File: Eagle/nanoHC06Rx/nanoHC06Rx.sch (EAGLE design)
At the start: 45 parts, among them J10 Relay, J14 Relay, J17 Relay, J2 Relay, J20 Pixel, J22 IR Rx, J33 Relay, Q1 2N5088, Q2 2N5088, X1 53047-11

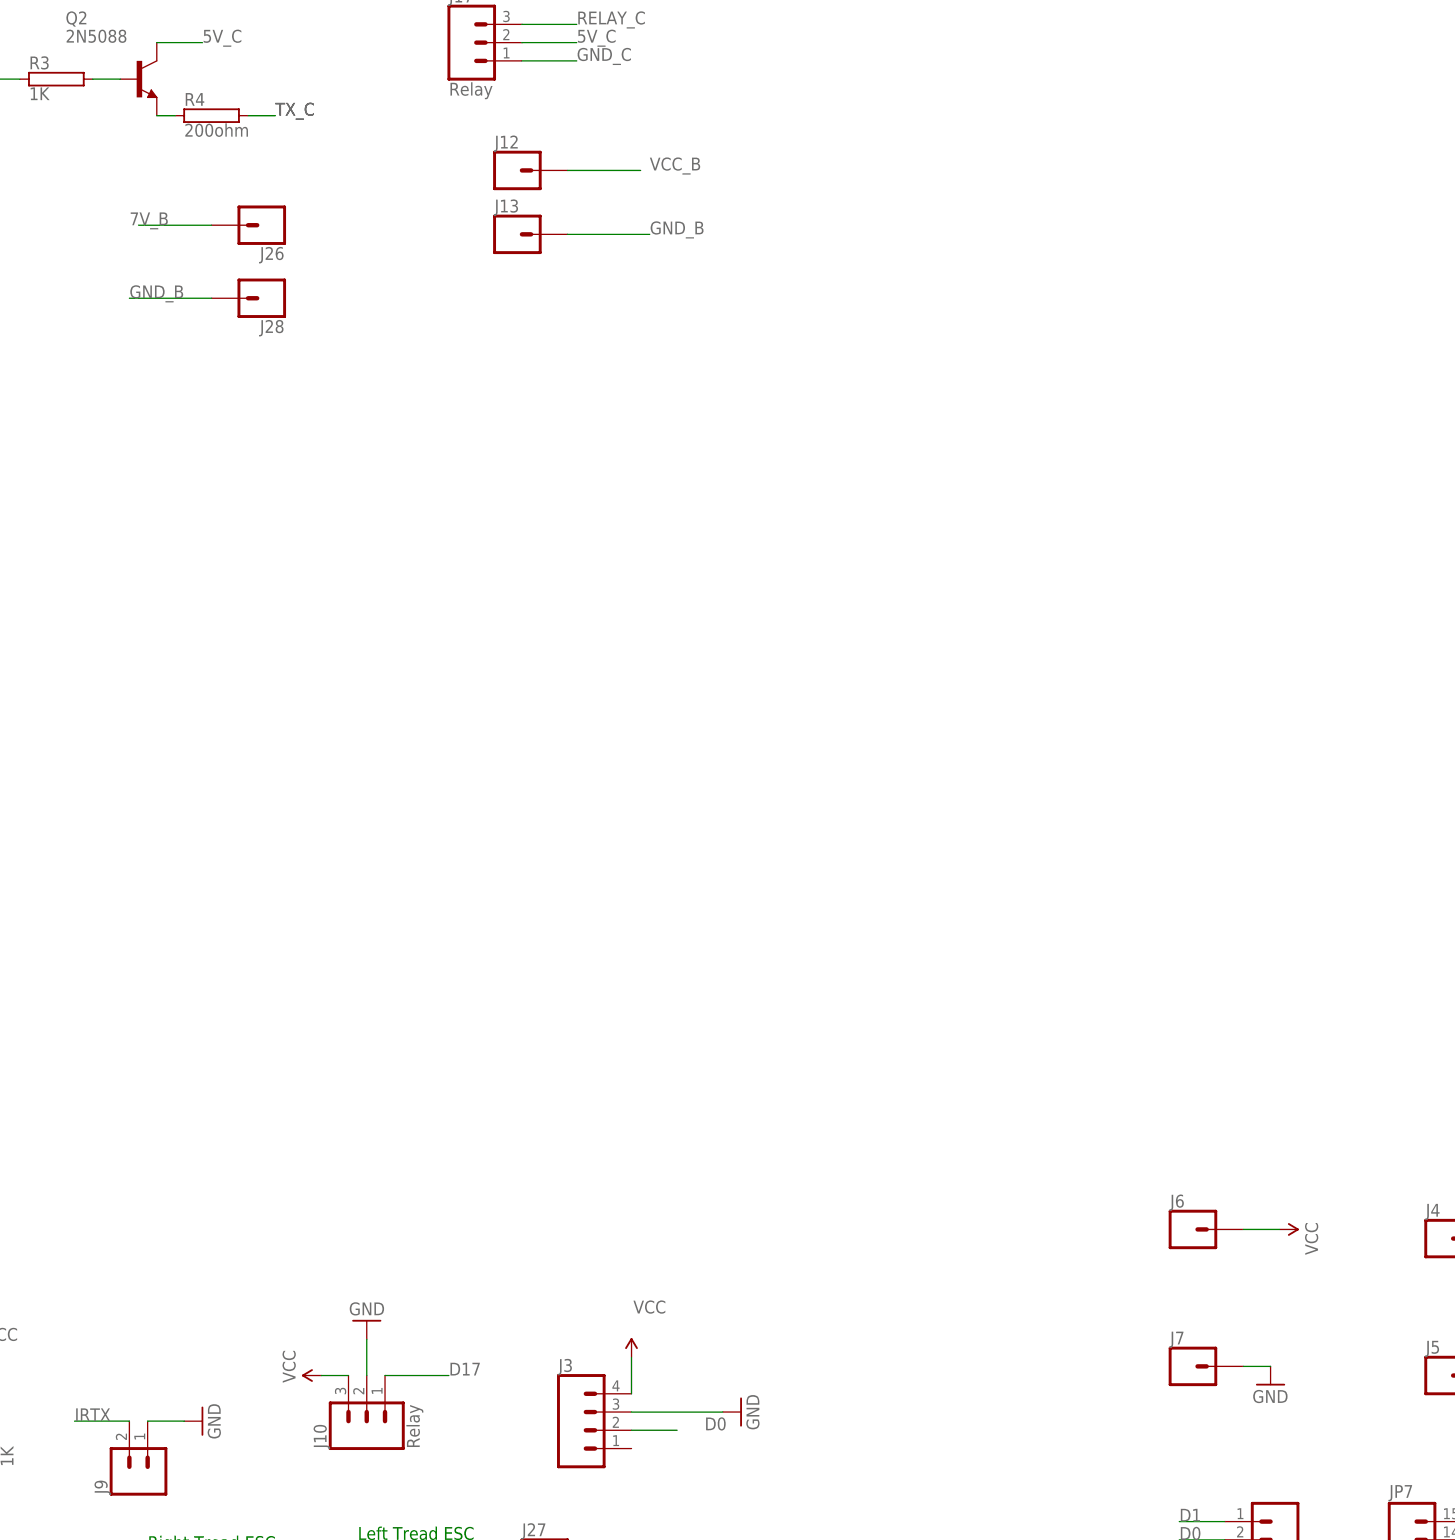
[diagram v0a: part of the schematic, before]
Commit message: Bind HC05 and HC06
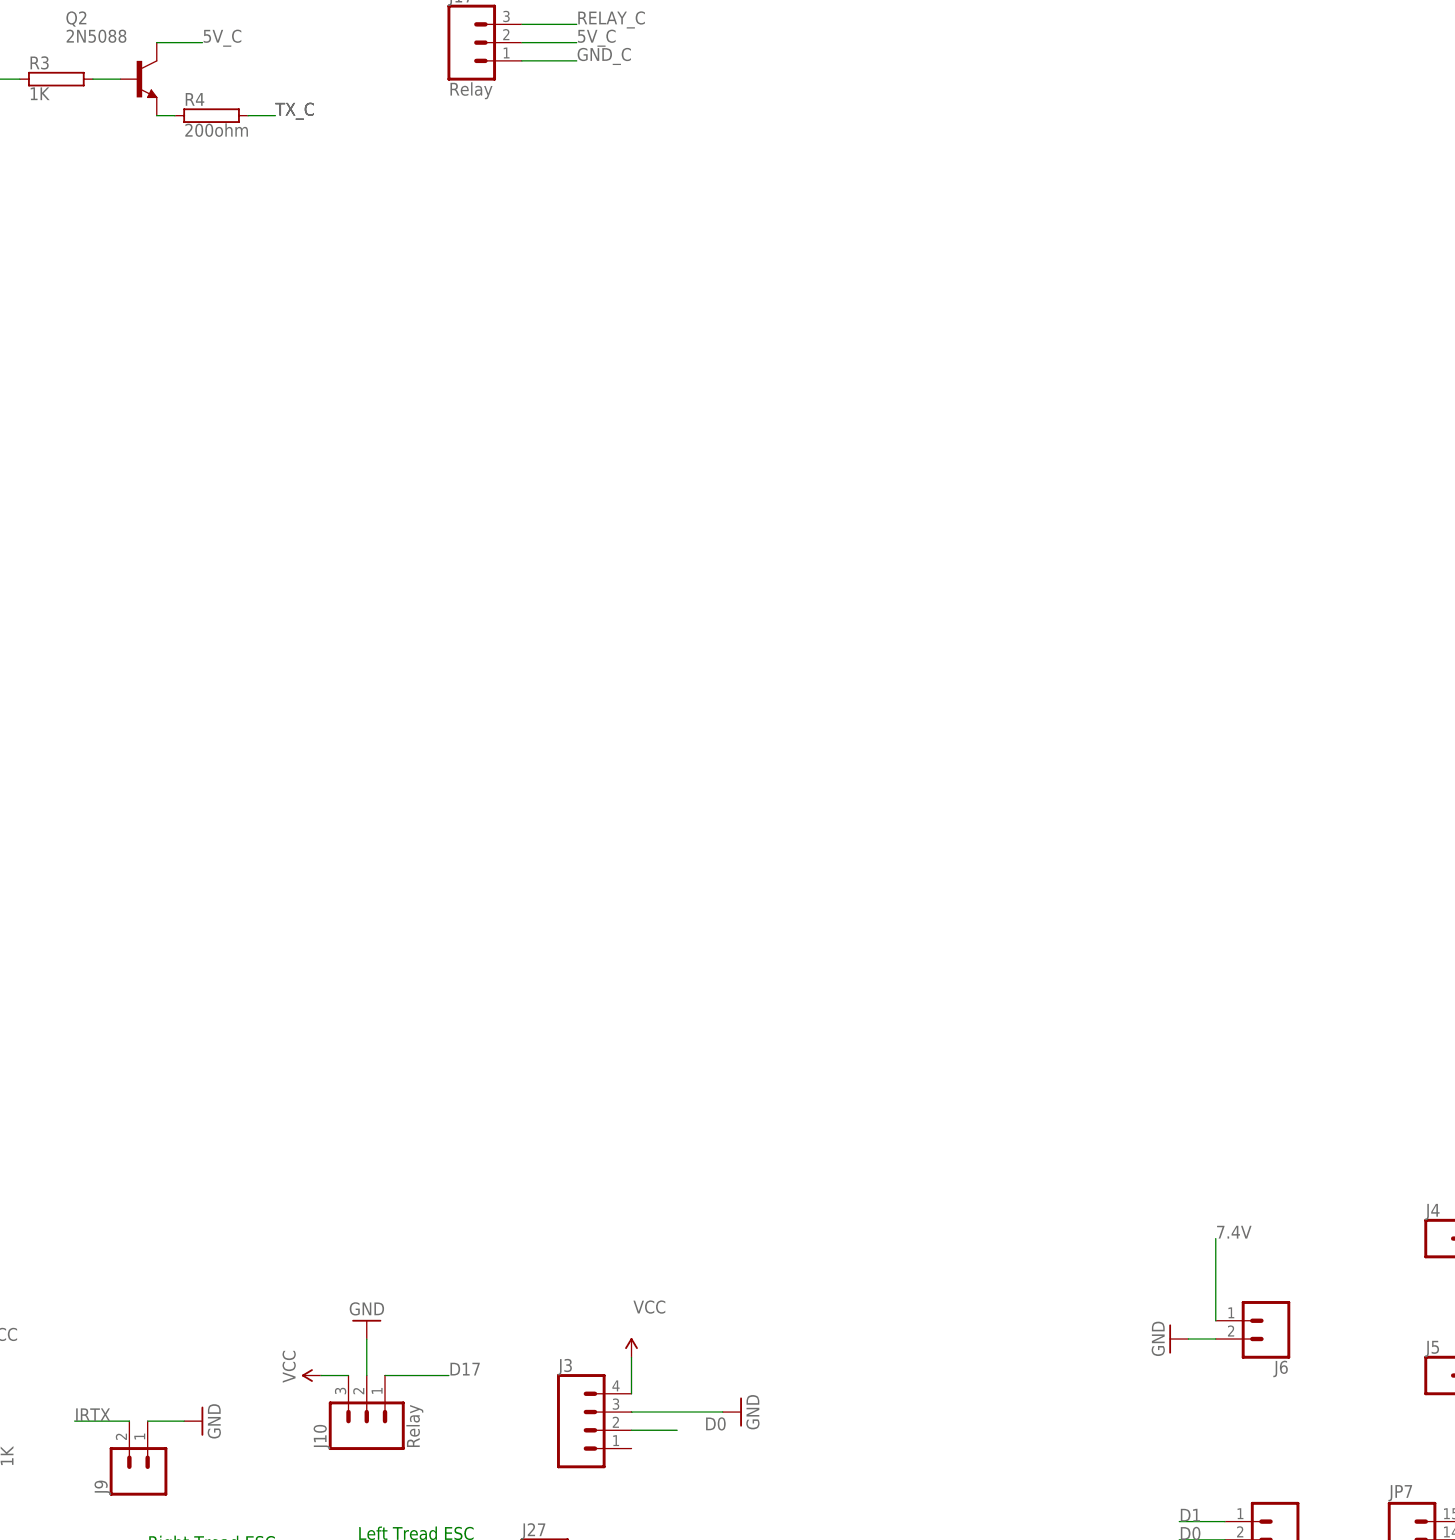
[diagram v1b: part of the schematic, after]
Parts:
- removed J12, J13, J26, J28, J7: (no value), SparkFun-Connectors:CONN_01
- J6: device SparkFun-Connectors:CONN_01 -> SparkFun-Connectors:CONN_02
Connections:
- removed net 7V_B: J26.1
- removed net GND_B: J13.1, J28.1
- removed net VCC_B: J12.1
- net 7.4V: now also J6.1
- net GND: now also J6.2; no longer J7.1
- net VCC: no longer J6.1
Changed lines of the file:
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@@
 <part name="J4" library="SparkFun-Connectors" library_urn="urn:adsk.eagle:library:513" deviceset="CONN_01" device="" package3d_urn="urn:adsk.eagle:package:38028/1"/>
 <part name="J5" library="SparkFun-Connectors" library_urn="urn:adsk.eagle:library:513" deviceset="CONN_01" device="" package3d_urn="urn:adsk.eagle:package:38028/1"/>
-<part name="J6" library="SparkFun-Connectors" library_urn="urn:adsk.eagle:library:513" deviceset="CONN_01" device="" package3d_urn="urn:adsk.eagle:package:38028/1"/>
-<part name="J7" library="SparkFun-Connectors" library_urn="urn:adsk.eagle:library:513" deviceset="CONN_01" device="" package3d_urn="urn:adsk.eagle:package:38028/1"/>
 <part name="GND6" library="SparkFun" deviceset="GND" device=""/>
-<part name="P+4" library="SparkFun" deviceset="VCC" device=""/>
-<part name="GND7" library="SparkFun" deviceset="GND" device=""/>
 <part name="JP3" library="SparkFun-Connectors" deviceset="M15" device=""/>
 <part name="JP4" library="SparkFun-Connectors" deviceset="M15" device=""/>
@@
 <part name="J32" library="SparkFun-Connectors" library_urn="urn:adsk.eagle:library:513" deviceset="CONN_10" device="&quot;" package3d_urn="urn:adsk.eagle:package:38157/1"/>
 <part name="J1" library="SparkFun-Connectors" library_urn="urn:adsk.eagle:library:513" deviceset="CONN_04" device="" package3d_urn="urn:adsk.eagle:package:38085/1"/>
-<part name="J12" library="SparkFun-Connectors" deviceset="CONN_01" device=""/>
-<part name="J13" library="SparkFun-Connectors" deviceset="CONN_01" device=""/>
 <part name="X1" library="con-molex" library_urn="urn:adsk.eagle:library:165" deviceset="53?-11" device="047" package3d_urn="urn:adsk.eagle:package:8078520/1"/>
 <part name="J16" library="SparkFun-Connectors" deviceset="CONN_06" device="NO_SILK_FEMALE_PTH"/>
@@
 <part name="J23" library="SparkFun-Connectors" library_urn="urn:adsk.eagle:library:513" deviceset="CONN_10" device="&quot;" package3d_urn="urn:adsk.eagle:package:38157/1"/>
 <part name="J24" library="SparkFun-Connectors" deviceset="CONN_08" device="&quot;"/>
-<part name="J26" library="SparkFun-Connectors" deviceset="CONN_01" device=""/>
-<part name="J28" library="SparkFun-Connectors" deviceset="CONN_01" device=""/>
 <part name="J29" library="SparkFun-Connectors" deviceset="CONN_06" device="NO_SILK_FEMALE_PTH"/>
 <part name="Q1" library="transistor-npn" library_urn="urn:adsk.eagle:library:398" deviceset="2N5088" device="" package3d_urn="urn:adsk.eagle:package:28523/2"/>
@@
 <part name="J14" library="SparkFun-Connectors" deviceset="CONN_03" device="" value="Relay"/>
 <part name="GND13" library="SparkFun" deviceset="GND" device=""/>
+<part name="J6" library="SparkFun-Connectors" deviceset="CONN_02" device=""/>
+<part name="GND7" library="SparkFun" deviceset="GND" device=""/>
 </parts>
 <sheets>
@@
 <attribute name="NAME" x="193.04" y="194.818" size="1.778" layer="95" font="vector"/>
 </instance>
-<instance part="J6" gate="G$1" x="160.02" y="212.09" smashed="yes">
-<attribute name="VALUE" x="157.48" y="207.264" size="1.778" layer="96" font="vector"/>
-<attribute name="NAME" x="157.48" y="215.138" size="1.778" layer="95" font="vector"/>
-</instance>
-<instance part="J7" gate="G$1" x="160.02" y="193.04" smashed="yes">
-<attribute name="VALUE" x="157.48" y="188.214" size="1.778" layer="96" font="vector"/>
-<attribute name="NAME" x="157.48" y="196.088" size="1.778" layer="95" font="vector"/>
-</instance>
 <instance part="GND6" gate="1" x="210.82" y="191.77" smashed="yes" rot="R90">
 <attribute name="VALUE" x="213.36" y="189.23" size="1.778" layer="96" rot="R90"/>
-</instance>
-<instance part="P+4" gate="1" x="172.72" y="212.09" smashed="yes" rot="R270">
-<attribute name="VALUE" x="176.276" y="213.106" size="1.778" layer="96" rot="R270"/>
-</instance>
-<instance part="GND7" gate="1" x="171.45" y="190.5" smashed="yes">
-<attribute name="VALUE" x="168.91" y="187.96" size="1.778" layer="96"/>
 </instance>
 <instance part="JP3" gate="G$1" x="261.62" y="353.06" smashed="yes" rot="R270">
@@
 <attribute name="NAME" x="249.682" y="401.32" size="1.778" layer="95" font="vector" rot="R90"/>
 </instance>
-<instance part="J12" gate="G$1" x="66.04" y="359.41" smashed="yes">
-<attribute name="VALUE" x="63.5" y="354.584" size="1.778" layer="96" font="vector"/>
-<attribute name="NAME" x="63.5" y="362.458" size="1.778" layer="95" font="vector"/>
-</instance>
-<instance part="J13" gate="G$1" x="66.04" y="350.52" smashed="yes">
-<attribute name="VALUE" x="63.5" y="345.694" size="1.778" layer="96" font="vector"/>
-<attribute name="NAME" x="63.5" y="353.568" size="1.778" layer="95" font="vector"/>
-</instance>
 <instance part="X1" gate="-1" x="38.1" y="410.21" smashed="yes">
 <attribute name="NAME" x="40.64" y="409.448" size="1.524" layer="95"/>
@@
 <attribute name="NAME" x="316.23" y="237.998" size="1.778" layer="95" font="vector"/>
 </instance>
-<instance part="J26" gate="G$1" x="31.75" y="351.79" smashed="yes" rot="R180">
-<attribute name="VALUE" x="34.29" y="356.616" size="1.778" layer="96" font="vector" rot="R180"/>
-<attribute name="NAME" x="34.29" y="348.742" size="1.778" layer="95" font="vector" rot="R180"/>
-</instance>
-<instance part="J28" gate="G$1" x="31.75" y="341.63" smashed="yes" rot="R180">
-<attribute name="VALUE" x="34.29" y="346.456" size="1.778" layer="96" font="vector" rot="R180"/>
-<attribute name="NAME" x="34.29" y="338.582" size="1.778" layer="95" font="vector" rot="R180"/>
-</instance>
 <instance part="J29" gate="G$1" x="43.18" y="137.16" smashed="yes" rot="R270">
 <attribute name="VALUE" x="33.274" y="142.24" size="1.778" layer="96" font="vector" rot="R270"/>
@@
 <instance part="GND13" gate="1" x="-1.27" y="154.94" smashed="yes" rot="R180">
 <attribute name="VALUE" x="1.27" y="157.48" size="1.778" layer="96" rot="R180"/>
+</instance>
+<instance part="J6" gate="G$1" x="171.45" y="199.39" smashed="yes" rot="R180">
+<attribute name="VALUE" x="173.99" y="204.216" size="1.778" layer="96" font="vector" rot="R180"/>
+<attribute name="NAME" x="173.99" y="193.802" size="1.778" layer="95" font="vector" rot="R180"/>
+</instance>
+<instance part="GND7" gate="1" x="157.48" y="196.85" smashed="yes" rot="R270">
+<attribute name="VALUE" x="154.94" y="199.39" size="1.778" layer="96" rot="R270"/>
 </instance>
 </instances>
@@
 </segment>
 <segment>
-<pinref part="J7" gate="G$1" pin="1"/>
-<pinref part="GND7" gate="1" pin="GND"/>
-<wire x1="171.45" y1="193.04" x2="167.64" y2="193.04" width="0.1524" layer="91"/>
-</segment>
-<segment>
 <pinref part="J27" gate="G$1" pin="1"/>
 <pinref part="GND8" gate="1" pin="GND"/>
@@
 <wire x1="55.88" y1="132.08" x2="50.8" y2="132.08" width="0.1524" layer="91"/>
 </segment>
+<segment>
+<pinref part="J6" gate="G$1" pin="2"/>
+<pinref part="GND7" gate="1" pin="GND"/>
+<wire x1="160.02" y1="196.85" x2="163.83" y2="196.85" width="0.1524" layer="91"/>
+</segment>
 </net>
 <net name="D3" class="0">
@@
 </segment>
 <segment>
-<pinref part="J6" gate="G$1" pin="1"/>
-<pinref part="P+4" gate="1" pin="VCC"/>
-<wire x1="172.72" y1="212.09" x2="167.64" y2="212.09" width="0.1524" layer="91"/>
-</segment>
-<segment>
 <pinref part="J27" gate="G$1" pin="2"/>
 <pinref part="P+5" gate="1" pin="VCC"/>
@@
 <label x="-12.7" y="148.59" size="1.778" layer="95"/>
 </segment>
+<segment>
+<pinref part="J6" gate="G$1" pin="1"/>
+<wire x1="163.83" y1="199.39" x2="163.83" y2="210.82" width="0.1524" layer="91"/>
+<label x="163.83" y="210.82" size="1.778" layer="95"/>
+</segment>
 </net>
 <net name="GND_D" class="0">
@@
 </segment>
 </net>
-<net name="VCC_B" class="0">
-<segment>
-<pinref part="J12" gate="G$1" pin="1"/>
-<wire x1="73.66" y1="359.41" x2="83.82" y2="359.41" width="0.1524" layer="91"/>
-<label x="85.09" y="359.41" size="1.778" layer="95"/>
-</segment>
-</net>
-<net name="GND_B" class="0">
-<segment>
-<pinref part="J13" gate="G$1" pin="1"/>
-<wire x1="73.66" y1="350.52" x2="85.09" y2="350.52" width="0.1524" layer="91"/>
-<label x="85.09" y="350.52" size="1.778" layer="95"/>
-</segment>
-<segment>
-<pinref part="J28" gate="G$1" pin="1"/>
-<wire x1="24.13" y1="341.63" x2="12.7" y2="341.63" width="0.1524" layer="91"/>
-<label x="12.7" y="341.63" size="1.778" layer="95"/>
-</segment>
-</net>
 <net name="LEFT_C" class="0">
 <segment>
@@
 </segment>
 </net>
-<net name="7V_B" class="0">
-<segment>
-<pinref part="J26" gate="G$1" pin="1"/>
-<wire x1="24.13" y1="351.79" x2="13.97" y2="351.79" width="0.1524" layer="91"/>
-<label x="12.7" y="351.79" size="1.778" layer="95"/>
-</segment>
-</net>

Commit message: eagle
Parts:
- removed J21: (no value), SparkFun-Connectors:CONN_02
- removed J22: IR Rx, SparkFun-Connectors:CONN_03
- removed Q2: 2N5088, transistor-npn:2N5088
- removed R3: 1K, resistor-power:RCA0001
- removed R4: 200ohm, resistor-power:RCA0001
- removed X1: 53047-11, con-molex:53047-11
- added C1: 10uF, SparkFun-Capacitors:10UF-POLAR-RADIAL-2.5MM-KIT-25V-20%
- added J12, J25, J26, J7: (no value), SparkFun-Connectors:CONN_06NO_SILK_FEMALE_PTH
- added J13, J15: (no value), SparkFun-Connectors:CONN_08"
- added J28: (no value), SparkFun-Connectors:CONN_01
- added J34: (no value), SparkFun-Connectors:CONN_04
- added PROG, PROG1, PROG2: (no value), SparkFun-Connectors:CONN_02
- added S3, S4: (no value), switch-omron:40-XX
- added U$1: V_REG_LD1117VXX, SparkFun-IC-Power:V_REG_LD1117VXX
- J16: value (none) -> Relay; device SparkFun-Connectors:CONN_06NO_SILK_FEMALE_PTH -> SparkFun-Connectors:CONN_03
- J20: value Pixel -> (none); device SparkFun-Connectors:CONN_03 -> SparkFun-Connectors:CONN_06NO_SILK_FEMALE_PTH
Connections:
- removed net 5V_C: J16.4, J17.2, J22.3, Q2.C, X1-2.S
- removed net 7.4V_C: J20.2, X1-3.S
- removed net DOWN_C: J16.1, X1-8.S
- removed net GND_C: J16.3, J17.1, J20.3, J21.2, J22.2, X1-1.S
- removed net LEFT_C: J16.6, X1-11.S
- removed net N$2: Q2.B, R3.2
- removed net N$4: Q2.E, R4.1
- removed net PIXEL_C: J20.1, X1-6.S
- removed net RELAY_C: J17.3, X1-7.S
- removed net RIGHT_C: J16.5, X1-10.S
- removed net RXIR_C: J22.1, X1-5.S
- removed net TXIR_C: R3.1, X1-4.S
- removed net TX_C: J21.1, R4.2
- removed net UP_C: J16.2, X1-9.S
- new net 3.3V_B: C1.+, J13.8, PROG1.1, PROG1.2, U$1.OUT
- new net 5V_B: J16.2, J17.2, J20.3, J34.1, PROG2.1, U$1.IN
- new net D4_D: JP4.7, S3.P
- new net D5_D: JP4.8, S4.P
- new net GND_B: C1.-, J13.1, J16.1, J17.3, J20.4, J20.6, J26.1, J26.2, J26.3, J26.4, J26.5, J26.6, J34.2, J7.6, U$1.GND
- new net GPIO02_B: J12.5, J15.7, J20.5
- new net GPIO04_B: J12.6, J15.8
- new net GPIO12_B: J12.1, J15.3, J17.1
- new net GPIO13_B: J12.2, J15.4
- new net GPIO14_B: J12.4, J15.6, J20.1
- new net GPIO15_B: J12.3, J15.5, J20.2
- new net GPIO16_B: J13.7, J16.3, J28.1
- new net PROG1: J13.5, PROG.1
- new net PROG2: J13.6, PROG.2
- new net UOR: J13.3, J34.3, J7.3
- new net UOT: J13.2, J7.2
- new net VCC_B: J15.1, J25.1, J25.2, J25.3, J25.4, J25.5, J25.6, J7.4, PROG2.2
- net GND_D: now also S3.S, S4.S
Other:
- moved on the sheet: J17

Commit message: esp32 bluetooth
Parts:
- removed JP19: (no value), SparkFun-Connectors:M15
- added J21, J22, J36, J38, J39: (no value), SparkFun-Connectors:CONN_01
- added J41, J43: Relay, SparkFun-Connectors:CONN_03
- J24: device SparkFun-Connectors:CONN_08" -> SparkFun-Connectors:CONN_01
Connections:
- new net BATT3.3V_B: J22.1, J24.1
- new net BATT_3V3_D: J38.1, J39.1
- net 3.3V_B: now also J36.1
- net 5V_B: now also J41.2, J43.2
- net GND_B: now also J21.1, J41.1, J43.3
- net GPIO13_B: now also J41.3
- net GPIO15_B: now also J43.1
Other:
- moved on the sheet: J11, J8
